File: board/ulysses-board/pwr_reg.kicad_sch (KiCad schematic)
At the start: 30 parts, among them J2 9V-30V / 10A, Q1 IRF9540N / BUZ11, SW1 On / Off, SW2 RESET, U1 LM350, U2 LM350, U3 LM350

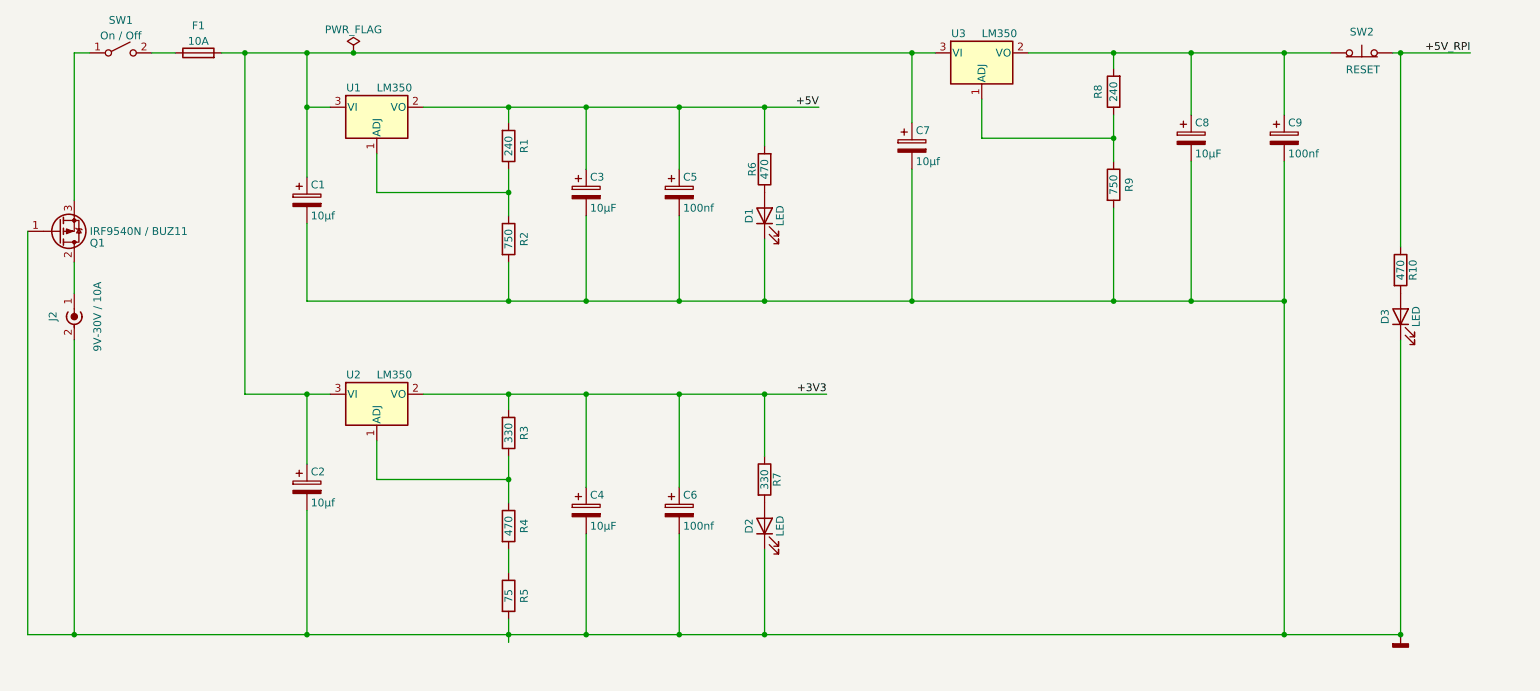
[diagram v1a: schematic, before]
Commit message: Add a ZVD protection to power circuit.
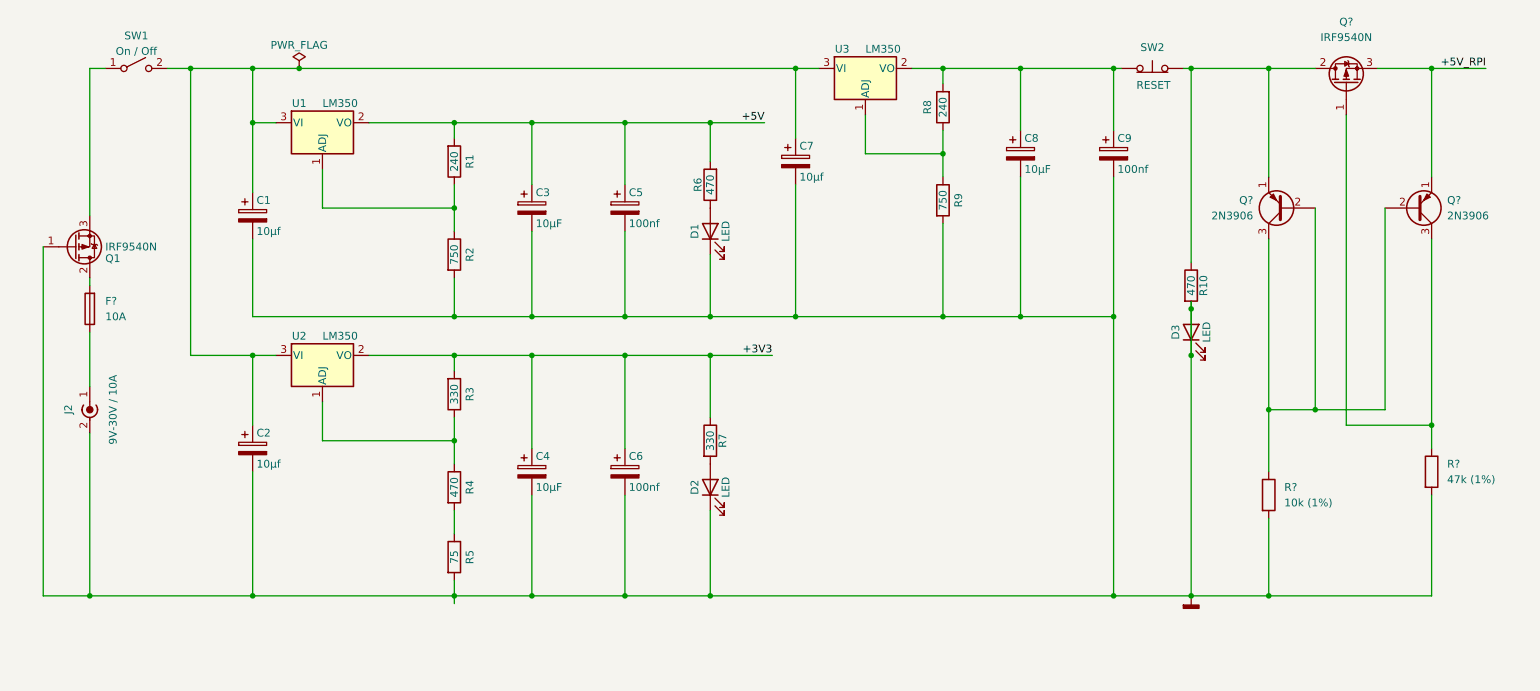
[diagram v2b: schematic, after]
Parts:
- removed F1: 10A, symbol Device:Fuse
- added F?: 10A, symbol Device:Fuse
- added Q? (x2): 2N3906, Package_TO_SOT_THT:TO-92_Inline, symbol Transistor_BJT:2N3906
- added Q?: IRF9540N, Package_TO_SOT_THT:TO-220-3_Vertical, symbol Transistor_FET:IRF9540N
- added R?: 10k (1%), symbol Device:R
- added R?: 47k (1%), symbol Device:R
- Q1: value IRF9540N / BUZ11 -> IRF9540N
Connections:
- net +5V_RPI: now also Q?.1 (E), Q?.3 (S); no longer R10.1, SW2.2 (B)
- net GNDD: now also D3.2 (A), R10.2, R?.2, R?.2
- net at C1.1, C2.1, C7.1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: now also SW1.2 (B)
- net at J2.1 (In): now also F?.1; no longer Q1.2 (D)
- new net: F?.2, Q1.2 (D)
- new net: Q?.1 (E), Q?.2 (D), R10.1, SW2.2 (B)
- new net: Q?.2 (B), Q?.2 (B), Q?.3 (C), R?.1
- new net: Q?.1 (G), Q?.3 (C), R?.1
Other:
- moved on the sheet: C1, C2, C3, C4, C5, C6, C7, C8, C9, D1, D2, D3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

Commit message: Make schemaics more readable.
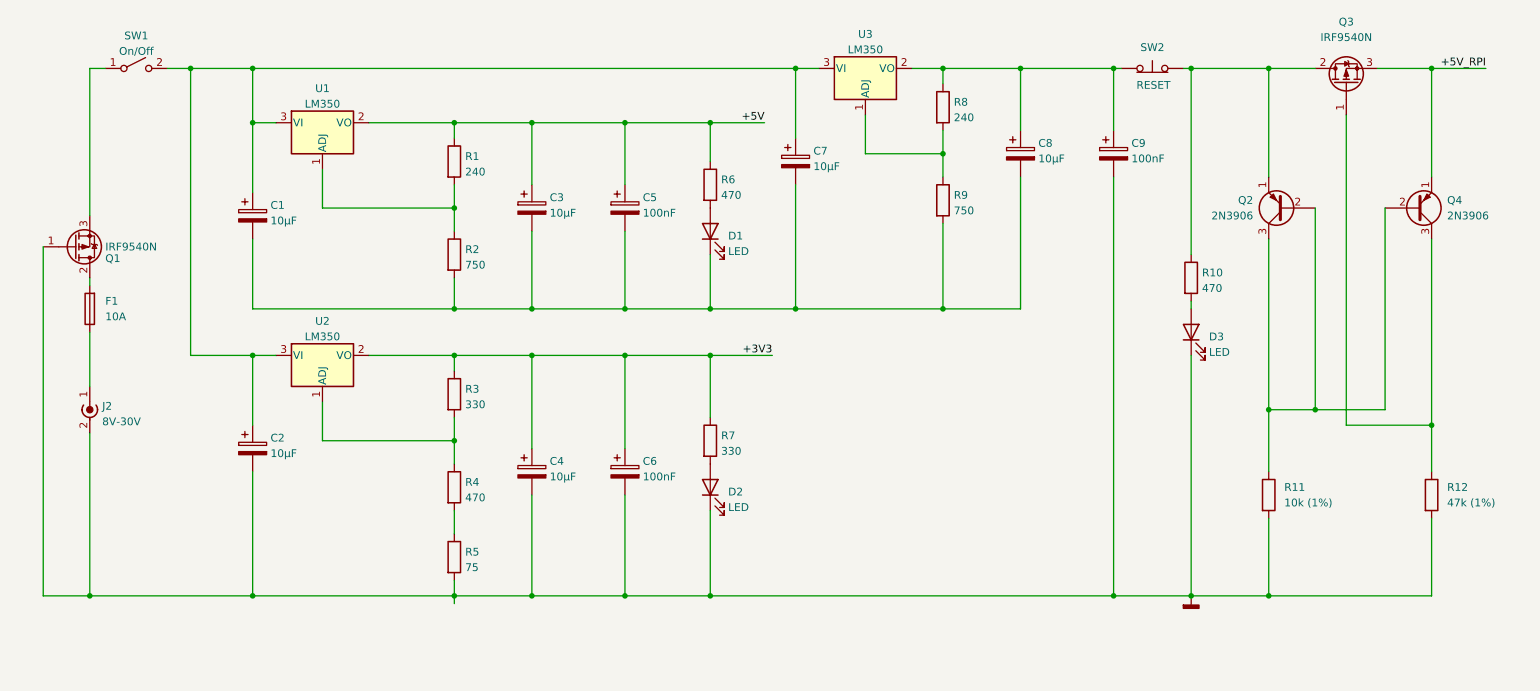
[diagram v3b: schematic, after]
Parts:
- C1, C2, C7: value 10µf -> 10µF; footprint Capacitor_THT:CP_Radial_D8.0mm_P2.50mm -> (none)
- C3, C4, C8: footprint Capacitor_THT:CP_Radial_D8.0mm_P2.50mm -> (none)
- C5, C6, C9: value 100nf -> 100nF; footprint Capacitor_THT:C_Axial_L3.8mm_D2.6mm_P7.50mm_Horizontal -> (none)
- D1, D2, D3: footprint LED_THT:LED_D1.8mm_W3.3mm_H2.4mm -> (none)
- J2: value 9V-30V / 10A -> 8V-30V
- SW1: value On / Off -> On/Off; footprint Button_Switch_SMD:SW_MEC_5GSH9 -> (none)
- gave numbers to parts that had none: 6
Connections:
- net +3V3: now also R3.1; no longer R3.2
- net +5V: now also R1.1, R6.1; no longer R1.2, R6.2
- net GNDD: no longer C1.2, C3.2, C5.2, C7.2, C8.2, D1.1 (K), D3.2 (A), R10.2, R2.2, R9.2
- net at D1.2 (A): now also R6.2; no longer R6.1
- net at C8.1, C9.1, SW2.1 (A)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: now also R8.1; no longer R8.2
- net at R4.1, U2.1 (ADJ): now also R3.2; no longer R3.1
- net at R9.1, U3.1 (ADJ): now also R8.2; no longer R8.1
- net at R2.1, U1.1 (ADJ): now also R1.2; no longer R1.1
- new net: D3.2 (A), R10.2
- new net: C1.2, C3.2, C5.2, C7.2, C8.2, D1.1 (K), R2.2, R9.2
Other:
- moved on the sheet: R12

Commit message: Some minor imptovements.
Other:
- moved on the sheet: C1, C2, C3, C4, C5, C6, C7, C8, C9, D1, D2, D3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
